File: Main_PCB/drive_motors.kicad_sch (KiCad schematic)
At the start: 10 parts, among them J401 Left_Encoder_Conn, J402 Left_Motor_Screw_Terminal, J403 SweepServo_Conn, J404 Right_Encoder_Conn, J405 Right_Motor_Screw_Terminal, U401 TB6612FNG

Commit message: First draft of schematic complete. Still need to verify it is correct before proceeding to pcb.
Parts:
- added R301: 10k, symbol Device:R
- J301: renamed from J403; value SweepServo_Conn -> Servo_Conn
- renumbered C401 to C301, C402 to C302, C403 to C303, C404 to C304, J401 to J302, J402 to J303, J404 to J304, J405 to J305, U401 to U301
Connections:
- net GNDPWR is gone; now on net GND: C303.2, C304.2, U301.10 (PGND2), U301.3 (PGND1), U301.4 (PGND1), U301.9 (PGND2)
- net +3.3V: no longer U301.19 (STBY)
- net GND: now also R301.2
- net +5V renamed +5V_Battery
- net SWEEP_PWM renamed SERVO_PWM
- new net STBY: R301.1, U301.19 (STBY)
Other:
- note added: "Note: 5V_Battery is used instead of 5V so that the servo is not powered by the USB connection if both USB and battery are connected at the same time. If the battery is not connected then the servo will not work."
- note removed: "Sweeper"
- note removed: "TODO: Add components to account for back-EMF from motor."
- moved on the sheet: J301

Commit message: Added decoupling capacitors, pulldown resistors, test points, and more. Still need to finish verifying schematic before PCB layout.
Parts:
- removed C303: 0.1uF, symbol Device:C
- removed C304: 10uF, symbol Device:C_Polarized
- added C303, C305: 470uF, symbol Device:C_Polarized
- added C304: 1uF, symbol Device:C
- added C306: 4.7uF, symbol Device:C
- added C307, C308, C309, C310: 100nF, symbol Device:C
- added R302, R303: 47k, symbol Device:R
- J303: value Left_Motor_Screw_Terminal -> Left_Motor_Terminal
- J305: value Right_Motor_Screw_Terminal -> Right_Motor_Terminal
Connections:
- net +5V_Battery: now also C305.1, C306.1, C307.1
- net +BATT: now also C303.1, C304.1, C308.1
- net A01: now also C309.1
- net A02: now also C309.2
- net B01: now also C310.1
- net B02: now also C310.2
- net GND: now also C303.2, C304.2, C305.2, C306.2, C307.2, C308.2, R302.2, R303.2
- net PWMA: now also R302.1
- net PWMB: now also R303.1
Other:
- note added: "Note: Place pulldown resistors R301, R302, R303 as close to their respective pin on the motor driver as possible so the inputs stay at a defined low level and are less susceptible to noise along the trace."
- moved on the sheet: J301, J302, J303, J304

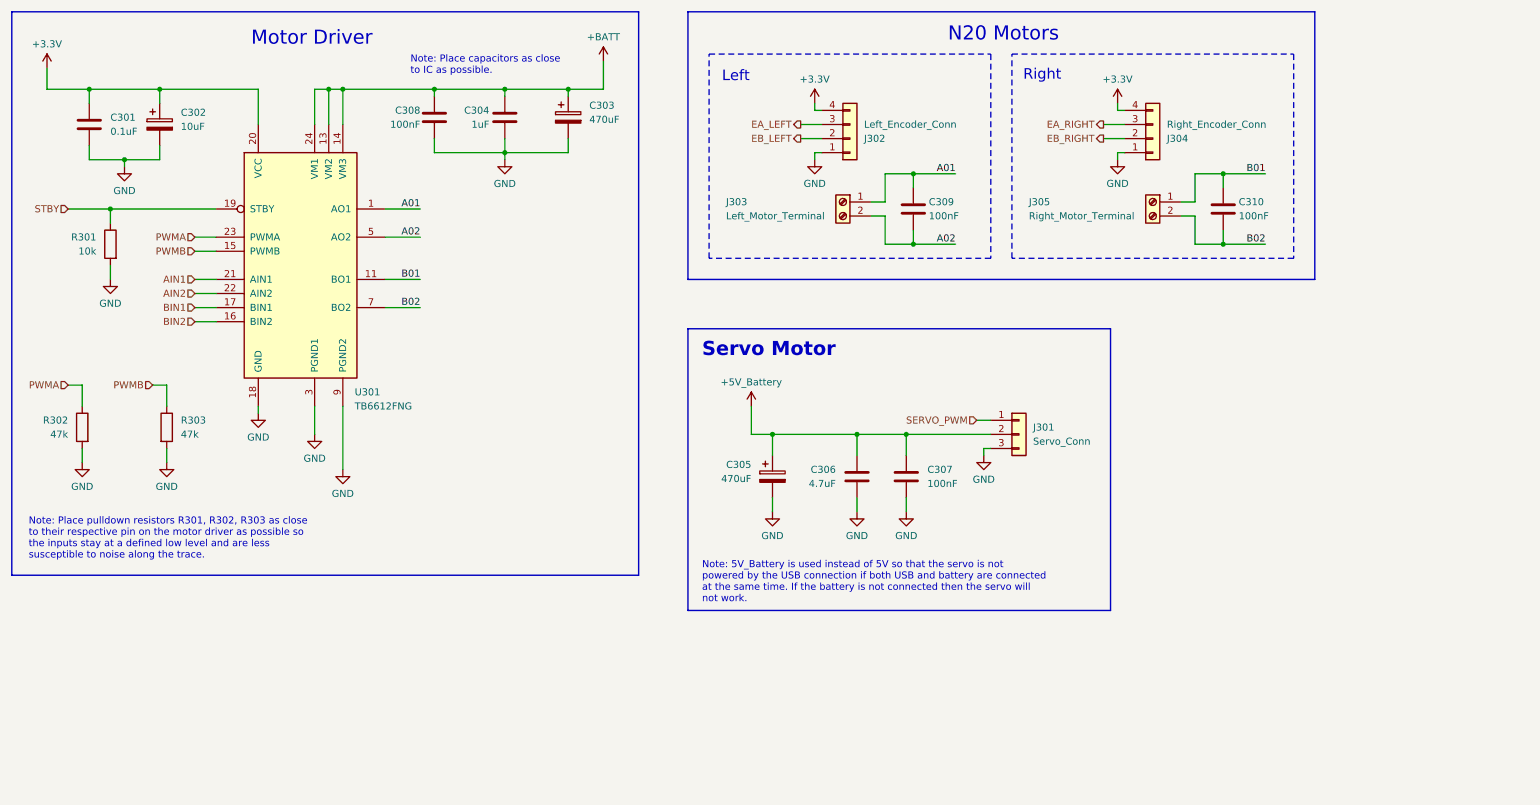
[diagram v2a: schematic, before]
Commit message: Adding most recent version of schematic. I have now decided to use NiMH batteries instead of Li-ion because they are safer and I don't want to start a fire.
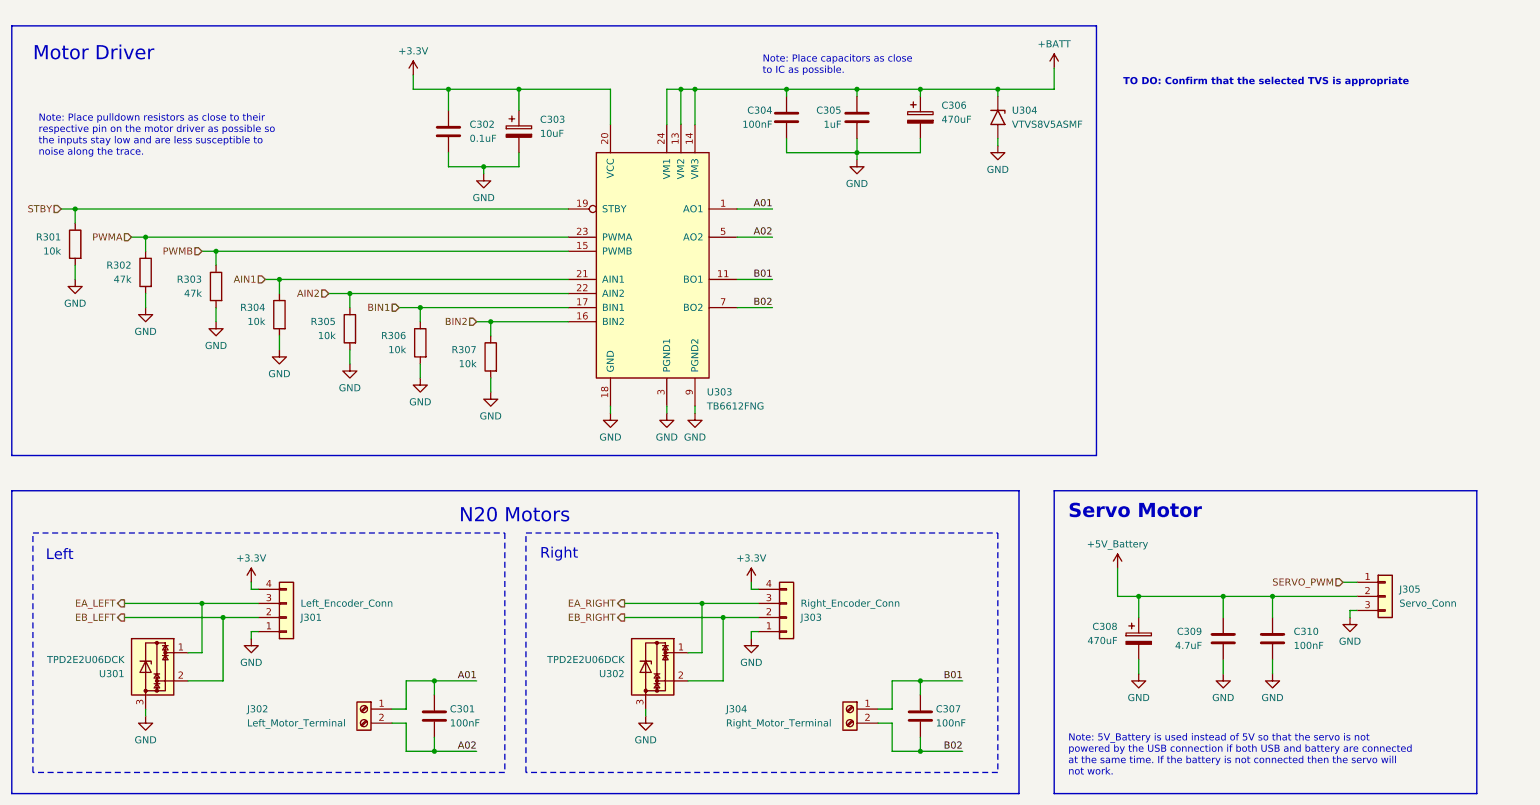
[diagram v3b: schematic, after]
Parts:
- removed J304: Right_Encoder_Conn, symbol Connector_Generic:Conn_01x04
- added J303: Right_Encoder_Conn, symbol Connector_Generic:Conn_01x04
- added R304, R305, R306, R307: 10k, symbol Device:R
- added U301, U302: TPD2E2U06DCK, Package_TO_SOT_SMD:SOT-323_SC-70, symbol Power_Protection:TPD2E2U06DCK
- added U304: VTVS8V5ASMF, symbol unidirectional_tvs:VTVS8V5ASMF
- renumbered C309 to C301, C301 to C302, C302 to C303, C308 to C304, C304 to C305, C303 to C306, C310 to C307, C305 to C308, C306 to C309, C307 to C310, J302 to J301, J303 to J302, J305 to J304, J301 to J305, U301 to U303
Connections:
- net +3.3V: now also J303.4 (Pin_4)
- net +BATT: now also U304.1 (A1)
- net AIN1: now also R304.1
- net AIN2: now also R305.1
- net BIN1: now also R306.1
- net BIN2: now also R307.1
- net EA_LEFT: now also U301.1
- net EA_RIGHT: now also J303.3 (Pin_3), U302.1
- net EB_LEFT: now also U301.2
- net EB_RIGHT: now also J303.2 (Pin_2), U302.2
- net GND: now also J303.1 (Pin_1), R304.2, R305.2, R306.2, R307.2, U301.3, U302.3, U304.2 (A2)
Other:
- note added: "Note: Place pulldown resistors as close to their respective pin on the motor driver as possible so the inputs stay low and are less susceptible to noise along the trace."
- note added: "TO DO: Confirm that the selected TVS is appropriate"
- note removed: "Note: Place pulldown resistors R301, R302, R303 as close to their respective pin on the motor driver as possible so the inputs stay at a defined low level and are less susceptible to noise along the trace."
- moved on the sheet: C301, C302, C303, C304, C305, C306, C307, C308, C309, C310, J301, J302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

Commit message: Adding changes. Changes made to cleanup schematic before pcb layout.
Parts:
- removed C302: 0.1uF, symbol Device:C
- removed C303: 10uF, symbol Device:C_Polarized
- removed C304, C310: 100nF, symbol Device:C
- removed C305: 1uF, symbol Device:C
- removed C306, C308: 470uF, symbol Device:C_Polarized
- removed C309: 4.7uF, symbol Device:C
- removed J305: Servo_Conn, symbol Connector_Generic:Conn_01x03
- removed R301, R304, R305, R306, R307: 10k, symbol Device:R
- removed R302, R303: 47k, symbol Device:R
- removed U303: TB6612FNG, Package_SO:SSOP-24_5.3x8.2mm_P0.65mm, symbol Driver_Motor:TB6612FNG
- removed U304: VTVS8V5ASMF, symbol unidirectional_tvs:VTVS8V5ASMF
- added C13: 0.01uF, symbol Device:C
- added C14: 10uF, symbol Device:C
- added C16, C17: 10uF/16V, symbol Device:C_Polarized
- added Q4: DMG3415U, symbol Simulation_SPICE:PMOS
- added R24, R25: 0.2R, symbol Device:R
- added U7: DRV8833PWP, Package_SO:HTSSOP-16-1EP_4.4x5mm_P0.65mm_EP3.4x5mm_Mask2.46x2.31mm_ThermalVias, symbol Driver_Motor:DRV8833PWP
- renumbered C301 to C15, C307 to C18, J301 to J5, J302 to J6, J303 to J7, J304 to J8, U301 to U6, U302 to U8
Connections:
- net +5V_Battery: now also Q4.1 (D)
- net AIN1: now also U7.16 (AIN1)
- net AIN2: now also U7.15 (AIN2)
- net BIN1: now also U7.9 (BIN1)
- net BIN2: now also U7.10 (BIN2)
- net GND: now also C14.1, C16.2, C17.2, Q4.2 (G), R24.2, R25.2, U7.13 (GND), U7.17 (GND)
- net A01 renamed AO1
- net AO1: now also U7.2 (AOUT1)
- net A02 renamed AO2
- net AO2: now also U7.4 (AOUT2)
- net B01 renamed BO1
- net BO1: now also U7.7 (BOUT1)
- net B02 renamed BO2
- net BO2: now also U7.5 (BOUT2)
- new net: C14.2, U7.14 (VINT)
- new net: C13.2, U7.11 (VCP)
- new net ASENSE: R24.1, U7.3 (AISEN)
- new net BSENSE: R25.1, U7.6 (BISEN)
- new net V_MOTOR: C13.1, C16.1, C17.1, Q4.3 (S), U7.12 (VM)
- new net ~{FAULT}: U7.8 (~{FAULT})
- new net ~{SLEEP}: U7.1 (~{SLEEP})
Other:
- note added: "Note: design based on Adafruit DRV8833 breakout board. Transistor is for reverse polarity protection. - protects circuit if battery is connected backwards"
- note removed: "Note: 5V_Battery is used instead of 5V so that the servo is not powered by the USB connection if both USB and battery are connected at the same time. If the battery is not connected then the servo will not work."
- note removed: "Note: Place capacitors as close to IC as possible."
- note removed: "Note: Place pulldown resistors as close to their respective pin on the motor driver as possible so the inputs stay low and are less susceptible to noise along the trace."
- note removed: "Servo Motor"
- note removed: "TO DO: Confirm that the selected TVS is appropriate"
